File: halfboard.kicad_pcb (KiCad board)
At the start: 4 copper layers, 117.4 x 86.6 mm, 52 parts, among them U1 

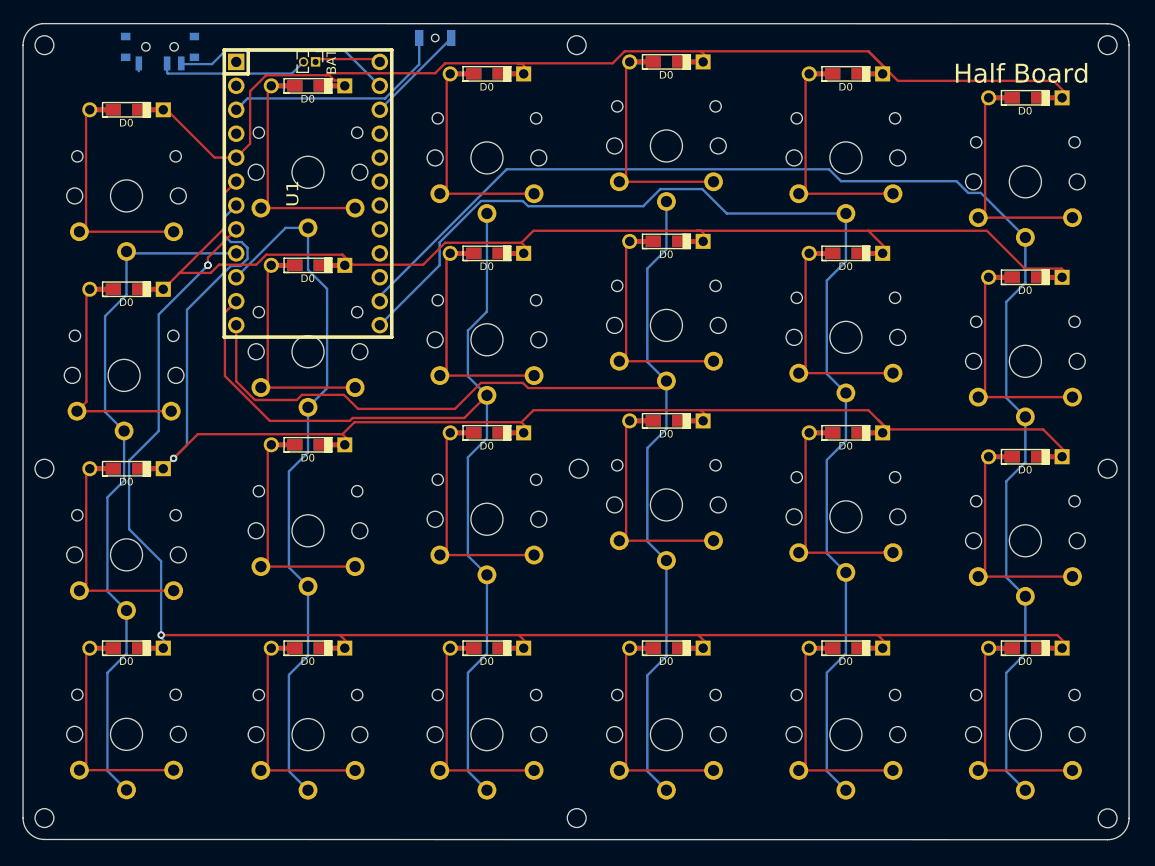
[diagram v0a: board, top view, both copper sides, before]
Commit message: add ground planes
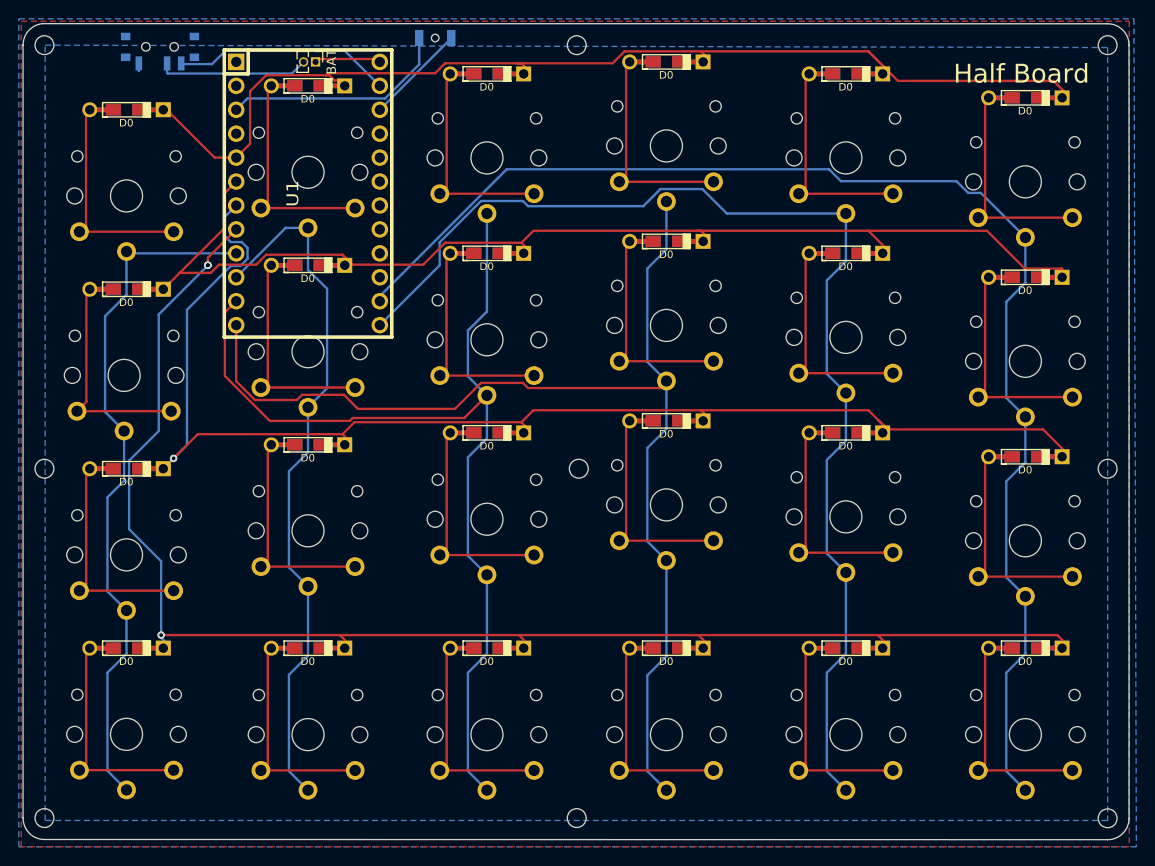
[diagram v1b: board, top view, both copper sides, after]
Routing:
- added copper zone on B.Cu, net (none)
- added copper zone on F.Cu, net (none)
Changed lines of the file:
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@@
-(kicad_pcb (version 20171130) (host pcbnew 5.1.9)
+(kicad_pcb (version 20171130) (host pcbnew "(5.1.8-0-10_14)")
   (general
     (thickness 1.6)
@@
     (visible_elements FFFFF7FF)
     (pcbplotparams
-      (layerselection 0x01fcf_ffffffff)
+      (layerselection 0x01fff_ffffffff)
       (usegerberextensions false)
       (usegerberattributes true)
@@
   (segment (start 83.39 49.792821) (end 79.774122 53.408699) (width 0.25) (layer B.Cu) (net 39))
   (segment (start 83.39 46.99) (end 83.39 49.792821) (width 0.25) (layer B.Cu) (net 39))
+  (zone (net 0) (net_name "") (layer B.Cu) (hatch edge 0.508)
+    (connect_pads (clearance 0.508))
+    (min_thickness 0.254)
+    (fill yes (arc_segments 32) (thermal_gap 0.508) (thermal_bridge_width 0.508))
+    (polygon
+      (pts
+        (xy 156.464 48.006) (xy 156.464 130.048) (xy 43.688 130.048) (xy 43.688 47.752)
+      )
+    )
+  )
+  (zone (net 0) (net_name "") (layer B.Cu) (hatch edge 0.508)
+    (connect_pads (clearance 0.508))
+    (min_thickness 0.254)
+    (fill yes (arc_segments 32) (thermal_gap 0.508) (thermal_bridge_width 0.508))
+    (polygon
+      (pts
+        (xy 159.512 132.842) (xy 40.894 132.842) (xy 40.894 44.958) (xy 159.258 44.958)
+      )
+    )
+  )
+  (zone (net 0) (net_name "") (layer F.Cu) (hatch edge 0.508)
+    (connect_pads (clearance 0.508))
+    (min_thickness 0.254)
+    (fill yes (arc_segments 32) (thermal_gap 0.508) (thermal_bridge_width 0.508))
+    (polygon
+      (pts
+        (xy 158.75 132.842) (xy 41.148 132.842) (xy 41.148 45.212) (xy 158.75 45.212)
+      )
+    )
+  )
 )

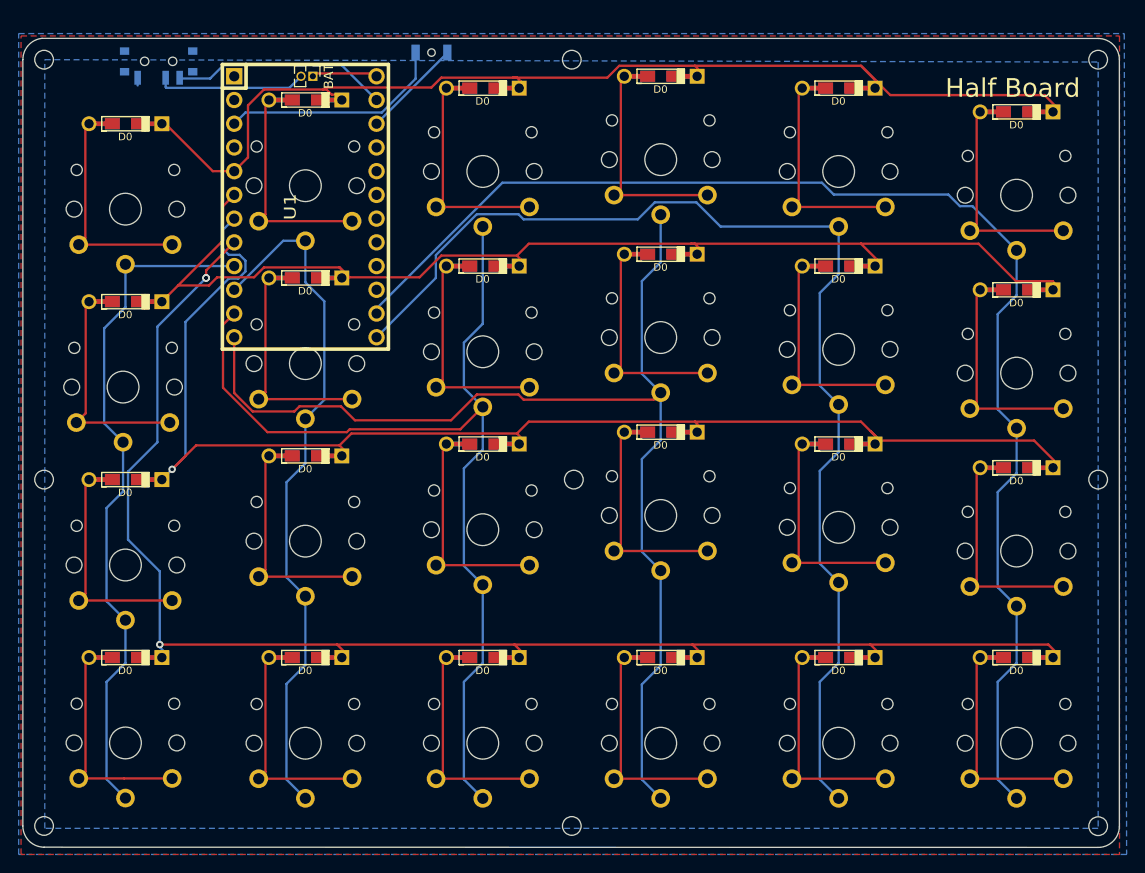
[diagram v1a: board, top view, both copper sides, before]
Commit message: add option to flip the board
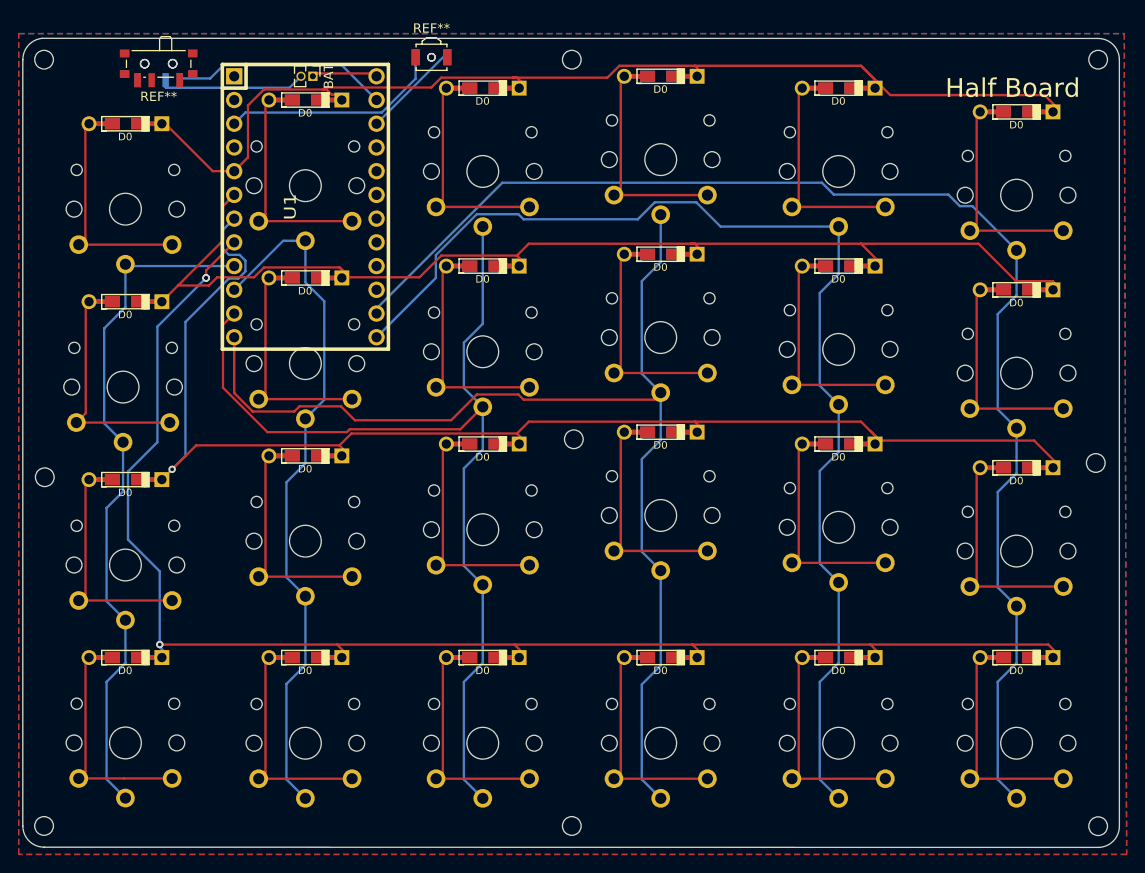
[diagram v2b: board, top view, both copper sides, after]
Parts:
- removed the REF** at (55.9, 48.3)
- added REF**: SW_SPST_B3U-3000P-B, Button_Switch_SMD:SW_SPST_B3U-3000P-B, F.Cu at (85.1, 47.5)
- added REF**: SW_SPDT_PCM12, Button_Switch_SMD:SW_SPDT_PCM12, F.Cu at (55.9, 48.5)
- added REF**: SW_SPDT_PCM12, Button_Switch_SMD:SW_SPDT_PCM12, B.Cu at (55.9, 48.5)
- moved REF** 0.51 mm to (85.1, 47.5)
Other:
- outline, holes or cut-outs redrawn

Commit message: Update PCB
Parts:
- removed the REF** at (55.9, 48.5) (x2)
- added REF**: SW_SPDT_PCM12, Button_Switch_SMD:SW_SPDT_PCM12, F.Cu at (55.9, 48.5)
- added REF**: SW_SPDT_PCM12, Button_Switch_SMD:SW_SPDT_PCM12, B.Cu at (55.9, 48.5)
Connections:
- REF** pad 1: (no net) -> RESET_GND
- REF** pad 2: (no net) -> RESET
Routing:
- net BAT_SW: track 16.0 -> 33.1 mm
- net BAT_GND: track 23.3 -> 34.2 mm, vias 0 -> 1
- net RESET_GND: track 24.2 -> 27.8 mm, vias 0 -> 1
- net RESET: track 10.8 -> 14.1 mm, vias 0 -> 1
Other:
- board size 117.4 x 86.6 mm -> 117.4 x 87.9 mm

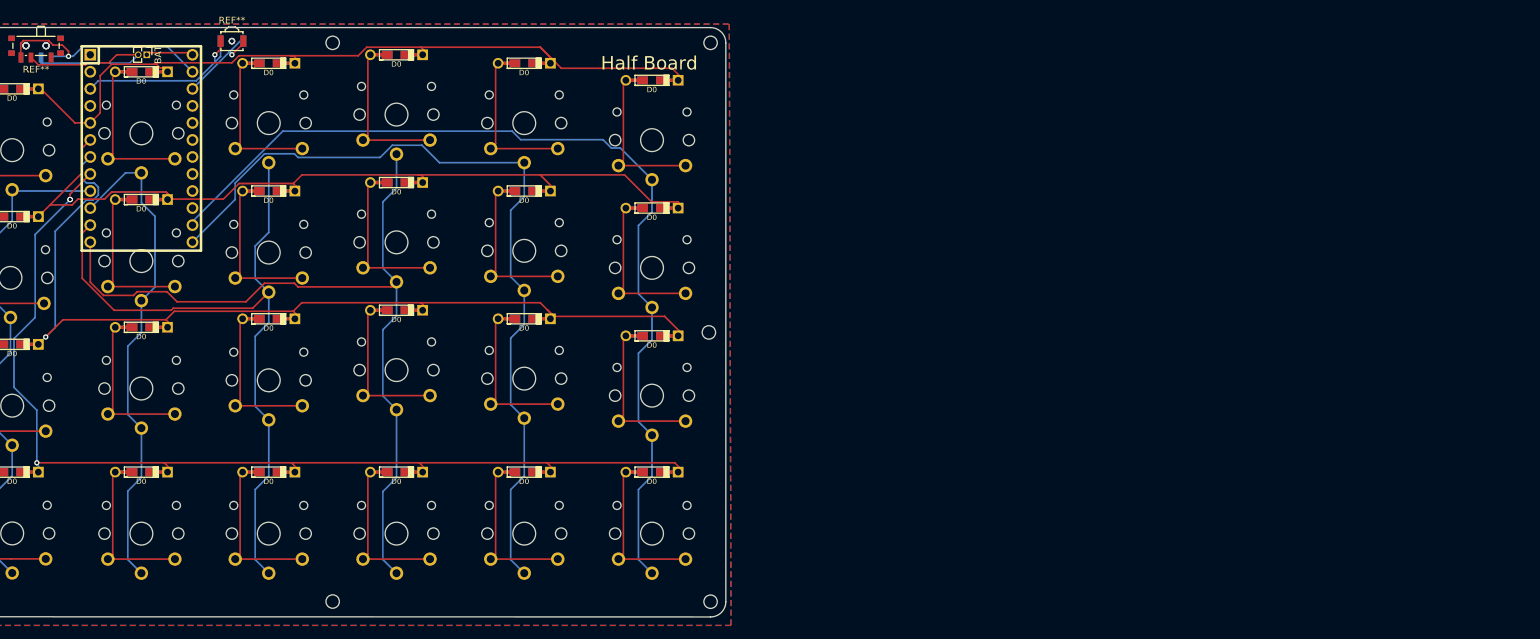
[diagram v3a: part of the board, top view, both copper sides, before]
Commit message: Add a bottom plate with mcu cut out
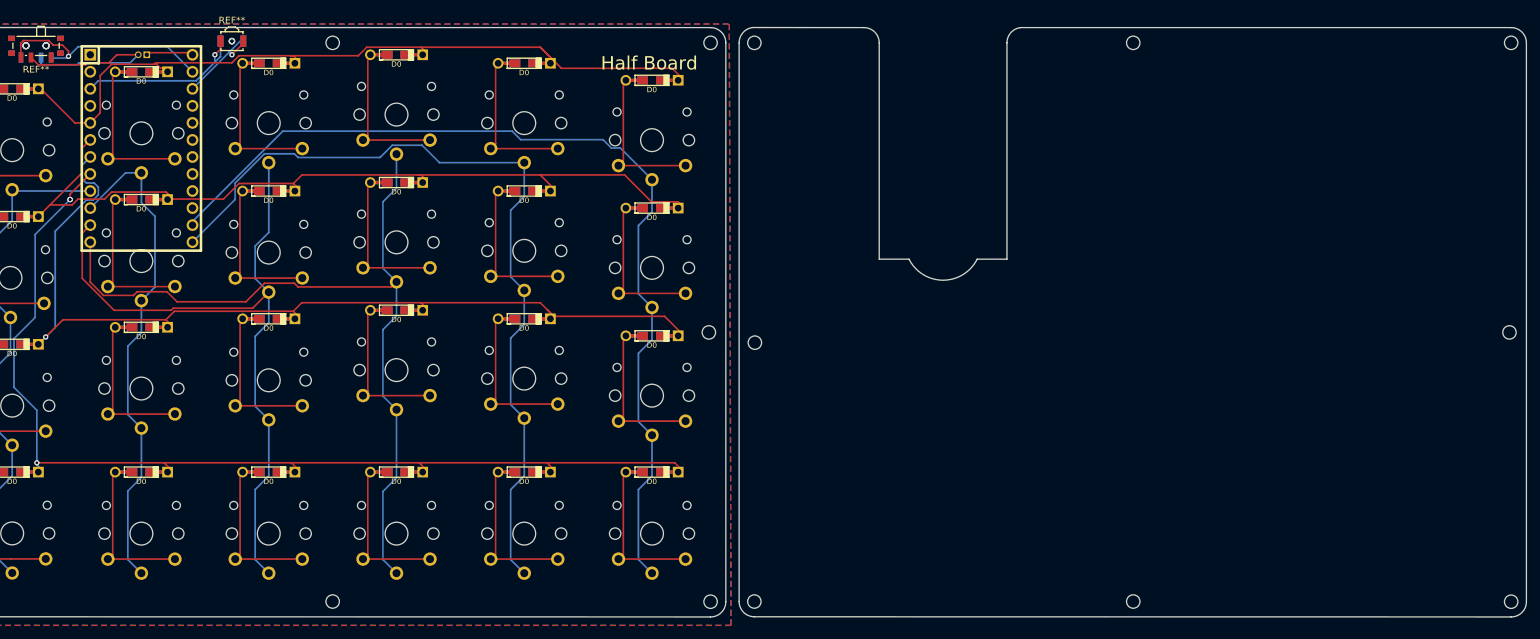
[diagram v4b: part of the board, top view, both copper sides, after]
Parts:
- removed the REF** at (55.9, 48.5) (x2)
- added REF**: SW_SPDT_PCM12, Button_Switch_SMD:SW_SPDT_PCM12, F.Cu at (55.9, 48.5)
- added REF**: SW_SPDT_PCM12, Button_Switch_SMD:SW_SPDT_PCM12, B.Cu at (55.9, 48.5)
- BAT: moved to B.Cu
- turned BAT to 90 degrees
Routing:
- net (no net): track 1.21 -> 0.00 mm
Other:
- board size 117.4 x 87.9 mm -> 236.8 x 87.9 mm

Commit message: update gerber files
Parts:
- removed BAT: PinHeader_1x02_P1.27mm_Vertical, Connector_PinHeader_1.27mm:PinHeader_1x02_P1.27mm_Vertical
- removed the REF** at (55.9, 48.5) (x2)
- added  : PinHeader_1x02_P2.54mm_Vertical, Connector_PinHeader_2.54mm:PinHeader_1x02_P2.54mm_Vertical, F.Cu at (73.7, 49.5)
- added REF**: SW_SPDT_PCM12, Button_Switch_SMD:SW_SPDT_PCM12, F.Cu at (55.9, 48.5)
- added REF**: SW_SPDT_PCM12, Button_Switch_SMD:SW_SPDT_PCM12, B.Cu at (55.9, 48.5)
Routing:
- net BAT0: track 7.07 -> 5.98 mm
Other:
- board size 236.8 x 87.9 mm -> 235.5 x 87.9 mm

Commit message: move gerber files to a folder
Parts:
- removed the   at (128.7, 78.8)
- removed the   at (128.7, 59.7)
- removed the   at (109.6, 58.4)
- removed the   at (109.6, 77.5)
- removed the   at (109.6, 96.5)
- removed the   at (90.6, 98.1)
- removed the   at (90.6, 79.0)
- removed the   at (90.6, 59.7)
- removed the   at (71.6, 61.2)
- removed the   at (71.6, 80.3)
- removed the   at (147.7, 62.3)
- removed the   at (71.6, 99.3)
- removed the   at (71.6, 120.9)
- removed the   at (52.3, 120.9)
- removed the   at (52.3, 101.9)
- removed the   at (147.7, 81.3)
- removed the   at (147.7, 100.4)
- removed the   at (147.7, 120.9)
- removed the   at (128.7, 120.9)
- removed the   at (109.6, 120.9)
- removed the   at (90.6, 120.9)
- removed the   at (128.7, 97.8)
- removed the D0 at (147.7, 53.3)
- removed the D0 at (128.7, 50.8)
- removed the D0 at (109.6, 49.5)
- removed the D0 at (109.6, 68.6)
- removed the D0 at (109.6, 87.6)
- removed the D0 at (90.6, 88.9)
- removed the D0 at (90.6, 69.8)
- removed the D0 at (90.6, 50.8)
- removed the D0 at (71.6, 52.1)
- removed the D0 at (71.6, 71.1)
- removed the D0 at (71.6, 90.2)
- removed the D0 at (147.7, 72.4)
- removed the D0 at (71.6, 111.8)
- removed the D0 at (52.3, 111.8)
- removed the D0 at (52.3, 92.7)
- removed the D0 at (147.7, 91.4)
- removed the D0 at (147.7, 111.8)
- removed the D0 at (128.7, 111.8)
- removed the D0 at (109.6, 111.8)
- removed the D0 at (90.6, 111.8)
- removed the D0 at (128.7, 88.9)
- removed the D0 at (128.7, 69.8)
- removed the REF** at (55.9, 48.5) (x2)
- added  : , mlp:Kailh-PG1350-1u-reversible-flip, F.Cu at (125.4, 78.8)
- added  : , mlp:Kailh-PG1350-1u-reversible-flip, F.Cu at (125.4, 59.7)
- added  : , mlp:Kailh-PG1350-1u-reversible-flip, F.Cu at (106.3, 58.4)
- added  : , mlp:Kailh-PG1350-1u-reversible-flip, F.Cu at (106.3, 77.5)
- added  : , mlp:Kailh-PG1350-1u-reversible-flip, F.Cu at (106.3, 96.5)
- added  : , mlp:Kailh-PG1350-1u-reversible-flip, F.Cu at (87.3, 98.1)
- added  : , mlp:Kailh-PG1350-1u-reversible-flip, F.Cu at (87.3, 79.0)
- added  : , mlp:Kailh-PG1350-1u-reversible-flip, F.Cu at (87.3, 59.7)
- added  : , mlp:Kailh-PG1350-1u-reversible-flip, F.Cu at (68.3, 61.2)
- added  : , mlp:Kailh-PG1350-1u-reversible-flip, F.Cu at (68.3, 80.3)
- added  : , mlp:Kailh-PG1350-1u-reversible-flip, F.Cu at (144.4, 62.3)
- added  : , mlp:Kailh-PG1350-1u-reversible-flip, F.Cu at (68.3, 99.3)
- added  : , mlp:Kailh-PG1350-1u-reversible-flip, F.Cu at (68.3, 120.9)
- added  : , mlp:Kailh-PG1350-1u-reversible-flip, F.Cu at (49.0, 120.9)
- added  : , mlp:Kailh-PG1350-1u-reversible-flip, F.Cu at (49.0, 101.9)
- added  : , mlp:Kailh-PG1350-1u-reversible-flip, F.Cu at (144.4, 81.3)
- added  : , mlp:Kailh-PG1350-1u-reversible-flip, F.Cu at (144.4, 100.4)
- added  : , mlp:Kailh-PG1350-1u-reversible-flip, F.Cu at (144.4, 120.9)
- added  : , mlp:Kailh-PG1350-1u-reversible-flip, F.Cu at (125.4, 120.9)
- added  : , mlp:Kailh-PG1350-1u-reversible-flip, F.Cu at (106.3, 120.9)
- added  : , mlp:Kailh-PG1350-1u-reversible-flip, F.Cu at (87.3, 120.9)
- added  : , mlp:Kailh-PG1350-1u-reversible-flip, F.Cu at (125.4, 97.8)
- added D0: D, mlp:Diode-dual, F.Cu at (144.4, 53.3)
- added D0: D, mlp:Diode-dual, F.Cu at (125.4, 50.8)
- added D0: D, mlp:Diode-dual, F.Cu at (106.3, 49.5)
- added D0: D, mlp:Diode-dual, F.Cu at (106.3, 68.6)
- added D0: D, mlp:Diode-dual, F.Cu at (106.3, 87.6)
- added D0: D, mlp:Diode-dual, F.Cu at (87.3, 88.9)
- added D0: D, mlp:Diode-dual, F.Cu at (87.3, 69.8)
- added D0: D, mlp:Diode-dual, F.Cu at (87.3, 50.8)
- added D0: D, mlp:Diode-dual, F.Cu at (68.3, 52.1)
- added D0: D, mlp:Diode-dual, F.Cu at (68.3, 71.1)
- added D0: D, mlp:Diode-dual, F.Cu at (68.3, 90.2)
- added D0: D, mlp:Diode-dual, F.Cu at (144.4, 72.4)
- added D0: D, mlp:Diode-dual, F.Cu at (68.3, 111.8)
- added D0: D, mlp:Diode-dual, F.Cu at (49.0, 111.8)
- added D0: D, mlp:Diode-dual, F.Cu at (49.0, 92.7)
- added D0: D, mlp:Diode-dual, F.Cu at (144.4, 91.4)
- added D0: D, mlp:Diode-dual, F.Cu at (144.4, 111.8)
- added D0: D, mlp:Diode-dual, F.Cu at (125.4, 111.8)
- added D0: D, mlp:Diode-dual, F.Cu at (106.3, 111.8)
- added D0: D, mlp:Diode-dual, F.Cu at (87.3, 111.8)
- added D0: D, mlp:Diode-dual, F.Cu at (125.4, 88.9)
- added D0: D, mlp:Diode-dual, F.Cu at (125.4, 69.8)
- added REF**: SW_SPDT_PCM12, Button_Switch_SMD:SW_SPDT_PCM12, F.Cu at (52.6, 48.5)
- added REF**: SW_SPDT_PCM12, Button_Switch_SMD:SW_SPDT_PCM12, B.Cu at (52.6, 48.5)
-  : value PinHeader_1x02_P2.54mm_Vertical -> (none)
- moved REF** 3.30 mm to (81.8, 47.5) (x2)
- moved   3.30 mm to (48.8, 82.8)
- moved   3.30 mm to (49.0, 63.8)
- moved D0 3.30 mm to (49.0, 73.7)
- moved D0 3.30 mm to (49.0, 54.6)
- moved   3.30 mm to (70.4, 49.5)
- moved U1 3.30 mm to (68.3, 63.5)
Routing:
- removed copper zone on B.Cu, net (none)
- removed copper zone on F.Cu, net (none)
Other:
- board size 235.5 x 87.9 mm -> 240.1 x 87.9 mm
- copper layers 4 -> 2
